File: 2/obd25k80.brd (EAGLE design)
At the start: 96.5 x 50.8 mm, 49 parts, among them IC1 PIC18F25K80, IC2 MCP25621, IC3 78L05, IC4 78L05, IC5 AP7384-3.3, IC6 ULN2003AN, J1 MA04-1, J2 DB9-M, Q1 BC557, X1 4Mhz

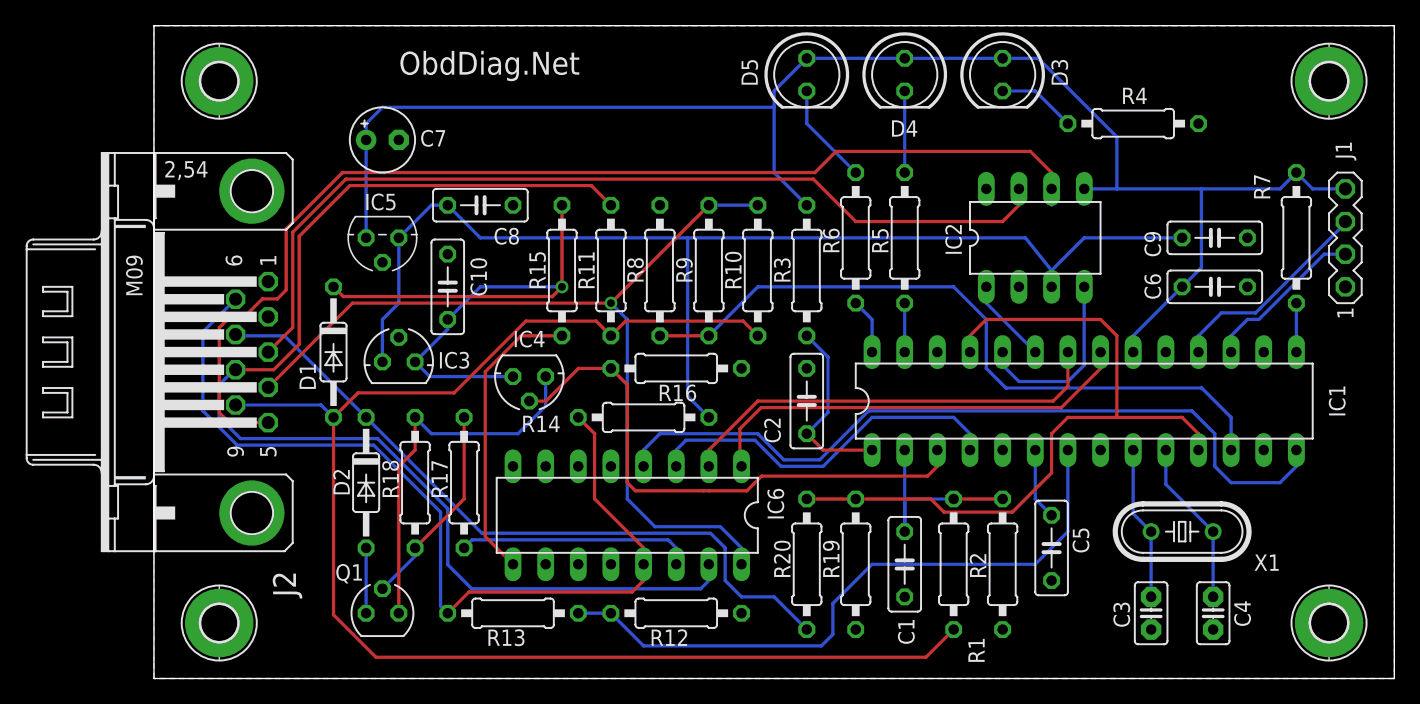
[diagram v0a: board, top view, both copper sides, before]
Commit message: Updated with resistor arrays
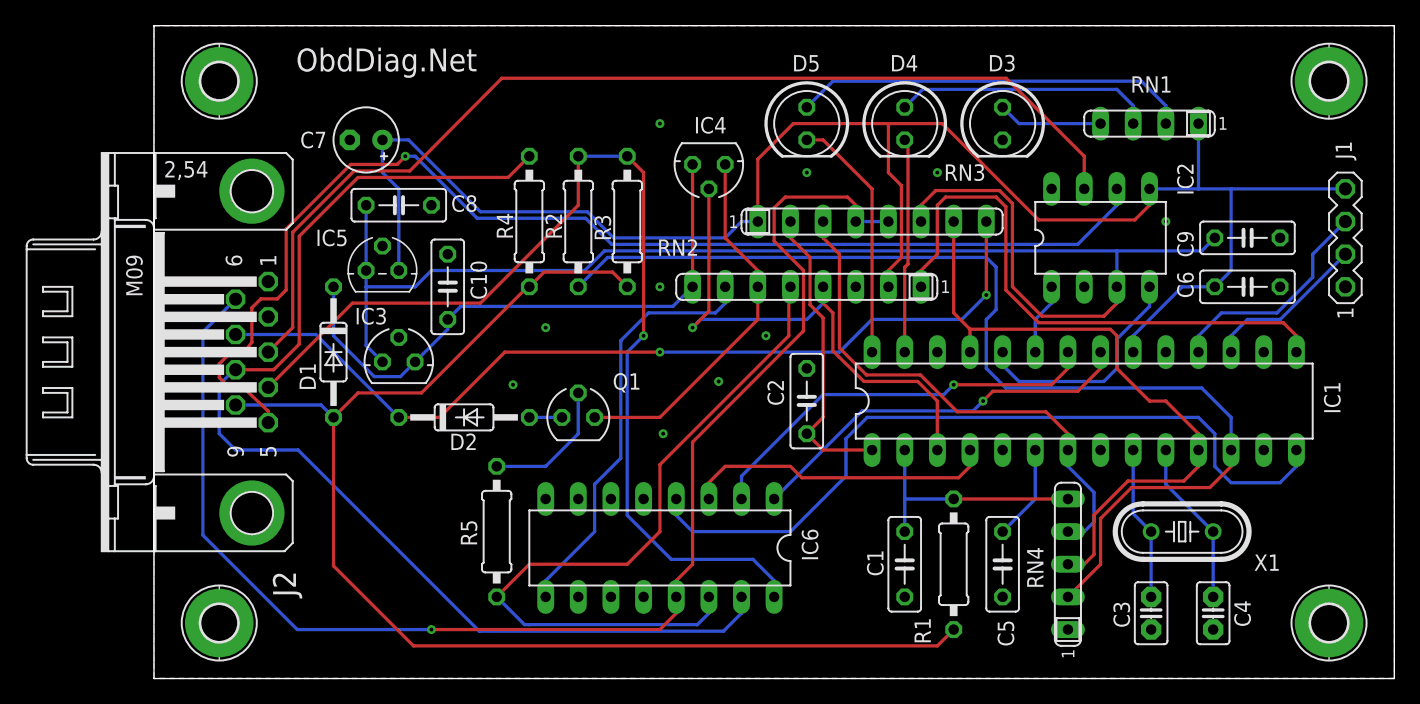
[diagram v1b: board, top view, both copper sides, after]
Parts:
- removed R10, R11: 510, rcl:0207/10
- removed R12, R19: 15K, rcl:0207/10
- removed R13, R14, R20: 22K, rcl:0207/10
- removed R15, R16, R18, R7: 10K, rcl:0207/10
- removed R17: 4.7K, rcl:0207/10
- removed R6: 330, rcl:0207/10
- removed R8: 18K, rcl:0207/10
- removed R9: 47K, rcl:0207/10
- added RN1: 330, resistor-sil:SIL4
- added RN2: 10K, resistor-sil:SIL8
- added RN3: 15K, resistor-sil:SIL8
- added RN4: 10K, resistor-sil:SIL5
- C7: value 2.2uF -> 1.5uF
- Q1: value BC557 -> BS250; device transistor-small-signal:SOT54A -> transistor-small-signal:SOT54E
- R1: value 47K -> 82K
- R2: value 6.2K -> 27K
- R3: value 10K -> 510
- R4: value 330 -> 510
- R5: value 330 -> 2.2K
- moved R4 47.6 mm to (29.2, 35.6), turned to 270 degrees
- moved R2 42.4 mm to (33.0, 35.6), turned to 90 degrees
- moved R5 39.1 mm to (26.7, 11.4)
- moved IC4 21.6 mm to (43.2, 40.0)
- moved Q1 21.6 mm to (33.0, 20.3)
- moved R3 14.5 mm to (36.8, 35.6)
- moved D2 9.16 mm to (24.1, 20.3), turned to 0 degrees
- moved C8 6.35 mm to (19.1, 36.8)
- moved IC2 5.08 mm to (73.7, 34.3)
- moved C5 4.02 mm to (66.0, 8.89)
- moved D3 3.81 mm to (66.0, 43.2)
- moved D4 3.81 mm to (58.4, 43.2)
- moved D5 3.81 mm to (50.8, 43.2)
- moved IC6 3.59 mm to (39.4, 10.2)
- moved C6 2.54 mm to (85.1, 30.5)
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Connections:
- removed net N$26: C1.1, IC1.2, R1.2, R2.1
- removed net N$30: Q1.B, R17.2, R18.1
- removed net N$32: D2.A, Q1.C
- new net N$5: D4.A, RN1.3
- new net N$8: D2.A, Q1.D
- new net N$9: C1.1, IC1.2, R1.2, RN4.5
- net +12V: now also RN2.8; no longer R15.2
- net +3V3: now also RN1.1, RN2.2, RN3.1; no longer D3.A, D4.A, D5.A, R3.1, R7.2
- net +5V: now also RN3.6; no longer R14.2
- net C2INB: now also RN3.3, RN4.4; no longer R12.2, R13.2
- net GND: now also D3.K, RN2.3, RN4.1; no longer R12.1, R16.1, R19.1, R2.2, R4.1, R8.2
- net ISO-K: now also R2.2, R3.1; no longer R10.1, R9.2
- net ISO-L: now also R4.1; no longer R11.1
- net J+DIV: now also RN3.7, RN4.3; no longer R19.2, R20.2
- net J1850+: now also RN3.8; no longer R20.1
- net J1850-: now also RN3.4, RN3.5; no longer R13.1, R14.1
- net N$1: now also D5.A, RN1.2; no longer D3.K, R4.2
- net N$10: now also Q1.G, R5.2; no longer D5.K, R6.2
- net N$11: now also D4.K; no longer R5.1
- net N$2: now also D5.K; no longer R6.1
- net N$25: now also R5.1, RN2.5; no longer R17.1
- net N$3: now also RN2.1; no longer R7.1
- net N$31: now also Q1.S, RN2.6; no longer Q1.E, R18.2
- net N$4: now also RN2.7; no longer R15.1
- net N$6: now also D3.A, RN1.4; no longer D4.K, R5.2
- net N$7: now also RN3.2; no longer R3.2
- net RA1: now also RN2.4; no longer R16.2
- net RC1: now also R2.1, RN4.2; no longer R8.1, R9.1
- net V+: now also R3.2, R4.2; no longer R10.2, R11.2
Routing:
- net N$3: track 3.81 -> 44.6 mm
- net N$25: track 18.3 -> 57.1 mm
- net J1850-: track 70.7 -> 107.2 mm, vias 0 -> 1
- net RC1: track 55.0 -> 85.4 mm
- net N$1: track 6.13 -> 31.0 mm
- net N$5: track 0.00 -> 20.3 mm
- net N$9: track 0.00 -> 19.1 mm
- net +5V: track 91.4 -> 109.6 mm
- net N$26: track 16.5 -> 0.00 mm
- net N$30: track 16.0 -> 0.00 mm
- net J1850+: track 55.4 -> 70.8 mm, vias 0 -> 2
- net N$2: track 4.34 -> 19.4 mm
- net +3V3: track 121.7 -> 136.1 mm
- net N$11: track 3.81 -> 16.7 mm
- net V+: track 111.5 -> 99.0 mm
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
